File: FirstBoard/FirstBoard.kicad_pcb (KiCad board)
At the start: 2 copper layers, 84.1 x 119.9 mm, 21 parts, among them J0 Battery, J1 MPU0, J10 MPU9, J11 MPU10, J12 MPU11, J13 MPU12, J15 SD_CARD, J2 MPU1, J3 MPU2, J4 MPU3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

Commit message: Finished V2
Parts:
- added R1: 10k, Resistor_THT:R_Axial_DIN0207_L6.3mm_D2.5mm_P10.16mm_Horizontal, F.Cu at (56.1, 179.2)
- added R4: 1K8, Resistor_THT:R_Axial_DIN0207_L6.3mm_D2.5mm_P10.16mm_Horizontal, F.Cu at (97.4, 178.8)
- added R5: 1K8, Resistor_THT:R_Axial_DIN0207_L6.3mm_D2.5mm_P10.16mm_Horizontal, F.Cu at (111.2, 178.8)
- added SW1: SW_Push, Button_Switch_THT:SW_PUSH_6mm_H5mm, F.Cu at (44.8, 179.0)
- added SW2: ON/OFF, TCC_FOOTPRINTS:BOTAO-ONOFF, F.Cu at (66.5, 148.2)
- J3: value MPU2 -> MPU3
- moved J15 97.1 mm to (75.5, 80.9), turned to 90 degrees
- moved D0 16.3 mm to (62.4, 178.6), turned to 90 degrees
- moved R3 12.0 mm to (80.0, 169.3), turned to -90 degrees
- moved R2 9.57 mm to (90.0, 169.3), turned to -90 degrees
- moved J0 8.51 mm to (75.8, 140.1), turned to 0 degrees
- moved D1 8.41 mm to (72.2, 178.8), turned to 90 degrees
- moved J13 5.13 mm to (44.7, 159.7)
- moved U2 1.91 mm to (84.4, 140.0), turned to 90 degrees
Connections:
- U1 pad 1: Net-(J14-Pad5) -> unconnected-(U1-Pad1)
- U1 pad 15: Net-(J14-Pad1) -> unconnected-(U1-Pad15)
- U1 pad 2: Net-(J14-Pad4) -> unconnected-(U1-Pad2)
- U1 pad 3: Net-(J14-Pad3) -> unconnected-(U1-Pad3)
- U1 pad 5: Net-(J14-Pad2) -> Switch
- U2 pad 1: BAT+ -> Net-(U2-Pad1)
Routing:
- net 3v3: track 189.0 -> 363.9 mm, vias 2 -> 0
- net Switch: track 0.00 -> 137.3 mm, vias 0 -> 2
- net SDA: track 157.1 -> 280.5 mm, vias 2 -> 6
- net SCL: track 169.4 -> 287.0 mm, vias 2 -> 4
- net LED_R: track 0.00 -> 98.8 mm, vias 0 -> 2
- net LED_G: track 0.00 -> 88.3 mm, vias 0 -> 2
- net AD0_12: track 11.1 -> 88.4 mm, vias 0 -> 2
- net MISO: track 79.4 -> 13.3 mm, vias 2 -> 0
- net INT: track 25.9 -> 84.0 mm
- net AD0_0: track 17.6 -> 74.9 mm, vias 0 -> 2
- net SCK: track 71.9 -> 16.9 mm, vias 2 -> 0
- net AD0_1: track 13.0 -> 63.7 mm, vias 0 -> 2
- net AD0_2: track 11.1 -> 58.1 mm, vias 0 -> 2
- net SS: track 63.6 -> 22.6 mm, vias 2 -> 0
- net MOSI: track 57.3 -> 17.5 mm, vias 2 -> 0
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- added copper zone on F.Cu, net GND
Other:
- board size 84.1 x 119.9 mm -> 82 x 122.1 mm

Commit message: Few pins adjusted
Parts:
- moved R4 24.6 mm to (118.3, 165.7), turned to 180 degrees
- moved R5 3.09 mm to (108.1, 178.5)
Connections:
- R4 pad 1: GND -> 3v3
- R5 pad 2: GND -> 3v3
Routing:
- net 3v3: track 363.9 -> 371.0 mm
- net SCL: track 287.0 -> 288.0 mm
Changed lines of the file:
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@@
   )
   (footprint "Resistor_THT:R_Axial_DIN0207_L6.3mm_D2.5mm_P10.16mm_Horizontal" (layer "F.Cu")
-    (at 111.22 178.76)
+    (at 108.14 178.46)
     (descr "Resistor, Axial_DIN0207 series, Axial, Horizontal, pin pitch=10.16mm, 0.25W = 1/4W, length*diameter=6.3*2.5mm^2, http://cdn-reichelt.de/documents/datenblatt/B400/1_4W%23YAG.pdf")
     (tags "Resistor Axial_DIN0207 series Axial Horizontal pin pitch 10.16mm 0.25W = 1/4W length 6.3mm diameter 2.5mm")
@@
       (net 8 "SCL") (pintype "passive"))
     (pad "2" thru_hole oval (at 10.16 0) (size 1.6 1.6) (drill 0.8) (layers *.Cu *.Mask)
-      (net 1 "GND") (pintype "passive"))
+      (net 6 "3v3") (pintype "passive"))
     (model "${KICAD6_3DMODEL_DIR}/Resistor_THT.3dshapes/R_Axial_DIN0207_L6.3mm_D2.5mm_P10.16mm_Horizontal.wrl"
       (offset (xyz 0 0 0))
@@
   )
   (footprint "Resistor_THT:R_Axial_DIN0207_L6.3mm_D2.5mm_P10.16mm_Horizontal" (layer "F.Cu")
-    (at 97.44 178.76)
+    (at 118.3 165.66 180)
     (descr "Resistor, Axial_DIN0207 series, Axial, Horizontal, pin pitch=10.16mm, 0.25W = 1/4W, length*diameter=6.3*2.5mm^2, http://cdn-reichelt.de/documents/datenblatt/B400/1_4W%23YAG.pdf")
     (tags "Resistor Axial_DIN0207 series Axial Horizontal pin pitch 10.16mm 0.25W = 1/4W length 6.3mm diameter 2.5mm")
@@
     (fp_line (start 1.93 1.25) (end 8.23 1.25) (layer "F.Fab") (width 0.1))
     (fp_line (start 8.23 -1.25) (end 1.93 -1.25) (layer "F.Fab") (width 0.1))
-    (pad "1" thru_hole circle (at 0 0) (size 1.6 1.6) (drill 0.8) (layers *.Cu *.Mask)
-      (net 1 "GND") (pintype "passive"))
-    (pad "2" thru_hole oval (at 10.16 0) (size 1.6 1.6) (drill 0.8) (layers *.Cu *.Mask)
+    (pad "1" thru_hole circle (at 0 0 180) (size 1.6 1.6) (drill 0.8) (layers *.Cu *.Mask)
+      (net 6 "3v3") (pintype "passive"))
+    (pad "2" thru_hole oval (at 10.16 0 180) (size 1.6 1.6) (drill 0.8) (layers *.Cu *.Mask)
       (net 7 "SDA") (pintype "passive"))
     (model "${KICAD6_3DMODEL_DIR}/Resistor_THT.3dshapes/R_Axial_DIN0207_L6.3mm_D2.5mm_P10.16mm_Horizontal.wrl"
@@
   (segment (start 75.478224 94.518224) (end 85.57 104.61) (width 1) (layer "B.Cu") (net 6))
   (segment (start 118.29 67.38) (end 118.29 84.84) (width 2) (layer "B.Cu") (net 6))
-  (segment (start 118.29 172.3) (end 118.29 154.82) (width 2) (layer "B.Cu") (net 6))
   (segment (start 44.725 119.57) (end 44.725 102.09) (width 2) (layer "B.Cu") (net 6))
+  (segment (start 118.29 172.3) (end 118.29 178.52) (width 2) (layer "B.Cu") (net 6))
   (segment (start 44.725 137.05) (end 44.725 131.955) (width 2) (layer "B.Cu") (net 6))
   (segment (start 75.840544 120.301065) (end 80.499479 124.96) (width 2) (layer "B.Cu") (net 6))
@@
   (segment (start 118.12 128.56) (end 118.29 128.39) (width 2) (layer "B.Cu") (net 6))
   (segment (start 118.29 119.84) (end 118.29 102.34) (width 2) (layer "B.Cu") (net 6))
+  (segment (start 118.29 163.08) (end 118.29 154.82) (width 2) (layer "B.Cu") (net 6))
   (segment (start 44.725 165.665) (end 44.725 172.465) (width 2) (layer "B.Cu") (net 6))
   (segment (start 44.77 165.71) (end 44.725 165.665) (width 1) (layer "B.Cu") (net 6))
+  (segment (start 118.29 172.3) (end 118.29 163.08) (width 2) (layer "B.Cu") (net 6))
   (segment (start 45.425 131.955) (end 44.725 131.955) (width 2) (layer "B.Cu") (net 6))
   (segment (start 84.62 124.96) (end 100.02 124.96) (width 2) (layer "B.Cu") (net 6))
@@
   (segment (start 75.840544 120.301065) (end 69.678935 120.301065) (width 2) (layer "B.Cu") (net 6))
   (segment (start 94.2848 111.1802) (end 94.2848 115.2952) (width 1) (layer "B.Cu") (net 6))
+  (segment (start 118.29 163.92) (end 118.29 163.08) (width 1) (layer "B.Cu") (net 6))
   (segment (start 44.725 159.66) (end 44.725 165.665) (width 2) (layer "B.Cu") (net 6))
   (segment (start 100.02 124.96) (end 103.62 128.56) (width 2) (layer "B.Cu") (net 6))
@@
   (segment (start 93.7402 85.7802) (end 94.2848 85.7802) (width 1) (layer "B.Cu") (net 7))
   (segment (start 52.345 159.66) (end 52.345 137.05) (width 1) (layer "B.Cu") (net 7))
-  (segment (start 110.67 175.69) (end 110.67 172.3) (width 1) (layer "B.Cu") (net 7))
-  (segment (start 107.6 178.76) (end 110.67 175.69) (width 1) (layer "B.Cu") (net 7))
+  (segment (start 108.14 165.66) (end 108.14 161.99) (width 1) (layer "B.Cu") (net 7))
   (segment (start 52.345 84.61) (end 52.345 79.235) (width 1) (layer "B.Cu") (net 7))
   (segment (start 110.67 84.84) (end 110.67 67.38) (width 1) (layer "B.Cu") (net 7))
@@
   (segment (start 110.67 119.84) (end 110.67 125.01) (width 1) (layer "B.Cu") (net 7))
   (segment (start 110.67 137.34) (end 110.67 154.82) (width 1) (layer "B.Cu") (net 7))
+  (segment (start 110.67 170.06) (end 110.67 172.3) (width 1) (layer "B.Cu") (net 7))
   (segment (start 96.4402 85.7802) (end 110.67 100.01) (width 1) (layer "B.Cu") (net 7))
   (segment (start 110.67 102.34) (end 110.67 100.31) (width 1) (layer "B.Cu") (net 7))
   (segment (start 110.67 134.46) (end 110.67 137.34) (width 1) (layer "B.Cu") (net 7))
+  (segment (start 108.14 161.99) (end 110.67 159.46) (width 1) (layer "B.Cu") (net 7))
   (segment (start 52.345 122.685) (end 52.345 119.57) (width 1) (layer "B.Cu") (net 7))
   (segment (start 90.92 82.96) (end 93.7402 85.7802) (width 1) (layer "B.Cu") (net 7))
@@
   (segment (start 89.92 77.76) (end 90.92 78.76) (width 1) (layer "B.Cu") (net 7))
   (segment (start 52.345 119.57) (end 52.345 102.09) (width 1) (layer "B.Cu") (net 7))
+  (segment (start 110.67 159.46) (end 110.67 170.06) (width 1) (layer "B.Cu") (net 7))
   (segment (start 57.62 73.06) (end 52.345 78.335) (width 1) (layer "B.Cu") (net 7))
   (segment (start 52.345 79.235) (end 52.345 67.13) (width 1) (layer "B.Cu") (net 7))
   (segment (start 110.67 119.84) (end 110.67 102.34) (width 1) (layer "B.Cu") (net 7))
+  (segment (start 110.67 154.82) (end 110.67 159.46) (width 1) (layer "B.Cu") (net 7))
   (segment (start 110.67 100.01) (end 110.67 100.31) (width 1) (layer "B.Cu") (net 7))
-  (segment (start 110.67 154.82) (end 110.67 172.3) (width 1) (layer "B.Cu") (net 7))
   (segment (start 113.21 132.47) (end 113.21 122.67) (width 1) (layer "F.Cu") (net 8))
   (segment (start 49.805 122.375) (end 49.805 132.675) (width 1) (layer "F.Cu") (net 8))
@@
   (segment (start 49.805 102.09) (end 49.805 119.57) (width 1) (layer "B.Cu") (net 8))
   (segment (start 113.21 122.67) (end 113.21 119.84) (width 1) (layer "B.Cu") (net 8))
-  (segment (start 113.21 175.75) (end 113.21 172.3) (width 1) (layer "B.Cu") (net 8))
   (segment (start 49.805 137.05) (end 49.805 159.66) (width 1) (layer "B.Cu") (net 8))
   (segment (start 94.2848 78.1602) (end 95.667089 78.1602) (width 1) (layer "B.Cu") (net 8))
@@
   (segment (start 49.805 119.57) (end 49.805 122.375) (width 1) (layer "B.Cu") (net 8))
   (segment (start 49.805 66.475) (end 49.805 67.13) (width 1) (layer "B.Cu") (net 8))
+  (segment (start 113.21 172.3) (end 113.21 173.44) (width 1) (layer "B.Cu") (net 8))
   (segment (start 113.21 102.34) (end 113.21 119.84) (width 1) (layer "B.Cu") (net 8))
+  (segment (start 113.16 173.44) (end 113.21 173.44) (width 1) (layer "B.Cu") (net 8))
   (segment (start 113.21 154.82) (end 113.21 137.34) (width 1) (layer "B.Cu") (net 8))
   (segment (start 96.96 76.867289) (end 96.96 64.4) (width 1) (layer "B.Cu") (net 8))
   (segment (start 49.805 67.13) (end 49.805 84.61) (width 1) (layer "B.Cu") (net 8))
-  (segment (start 111.22 178.76) (end 113.22 176.76) (width 1) (layer "B.Cu") (net 8))
-  (segment (start 113.22 175.76) (end 113.21 175.75) (width 1) (layer "B.Cu") (net 8))
   (segment (start 49.805 132.675) (end 49.805 137.05) (width 1) (layer "B.Cu") (net 8))
+  (segment (start 108.14 178.46) (end 113.16 173.44) (width 1) (layer "B.Cu") (net 8))
   (segment (start 113.21 84.84) (end 113.21 102.34) (width 1) (layer "B.Cu") (net 8))
   (segment (start 51.97 64.31) (end 49.805 66.475) (width 1) (layer "B.Cu") (net 8))
-  (segment (start 113.22 176.76) (end 113.22 175.76) (width 1) (layer "B.Cu") (net 8))
   (segment (start 113.21 67.38) (end 113.21 66.8) (width 1) (layer "B.Cu") (net 8))
   (segment (start 90.61 132.99) (end 90.61 106.32) (width 1) (layer "F.Cu") (net 9))

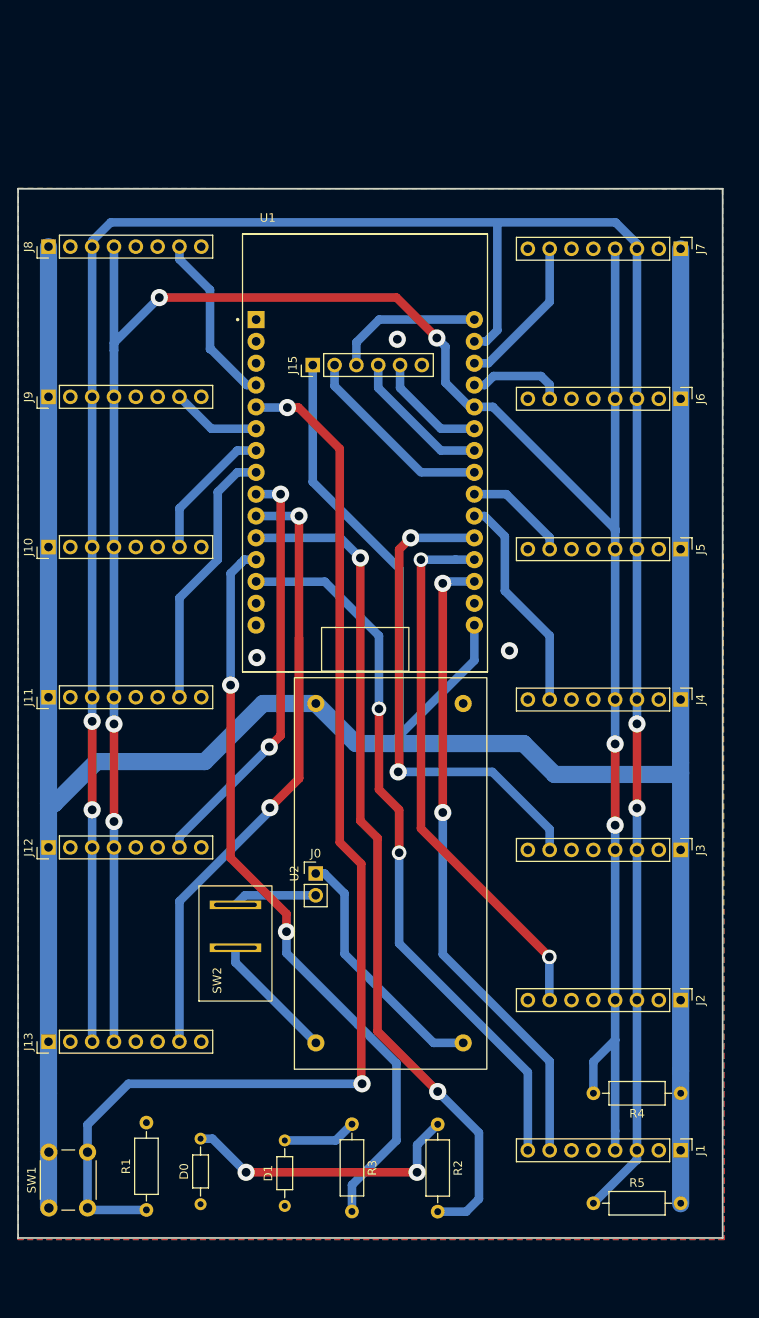
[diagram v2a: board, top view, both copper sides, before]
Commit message: bigger space between ESP and Source
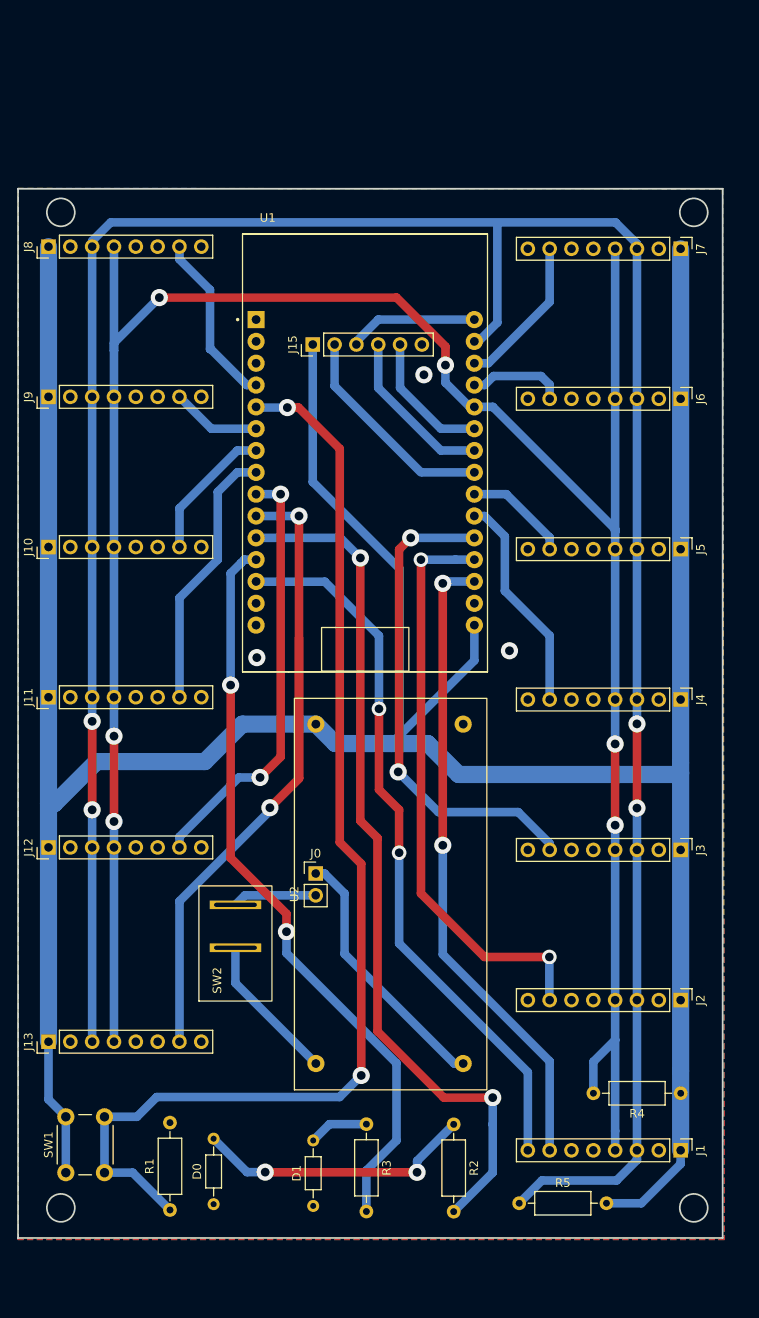
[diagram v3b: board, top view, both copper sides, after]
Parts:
- moved R5 8.64 mm to (99.5, 178.5)
- moved SW1 4.56 mm to (46.7, 174.9)
- moved D1 3.31 mm to (75.5, 178.8)
- moved R1 2.74 mm to (58.9, 179.2)
- moved U2 2.40 mm to (84.4, 142.5)
- moved J15 2.39 mm to (75.5, 78.5)
- moved R2 1.86 mm to (91.9, 169.3)
- moved R3 1.68 mm to (81.7, 169.3)
- moved D0 1.52 mm to (63.9, 178.6)
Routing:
- net SCL: track 288.0 -> 296.1 mm
- net AD0_1: track 63.7 -> 68.1 mm
- net Switch: track 137.3 -> 133.5 mm
- net 3v3: track 371.0 -> 373.8 mm
- net Net-(U2-Pad1): track 14.9 -> 17.3 mm
- net SS: track 22.6 -> 25.0 mm
- net SCK: track 16.9 -> 19.3 mm
- net MISO: track 13.3 -> 15.7 mm
- net MOSI: track 17.5 -> 15.1 mm
- net LED_R: track 98.8 -> 100.8 mm
- net Net-(D1-Pad2): track 8.60 -> 6.98 mm
- net AD0_11: track 48.8 -> 50.3 mm
- net BAT-: track 29.4 -> 30.4 mm
- net AD0_2: track 58.1 -> 57.1 mm
- net Net-(D0-Pad2): track 33.4 -> 32.6 mm
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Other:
- outline, holes or cut-outs redrawn
